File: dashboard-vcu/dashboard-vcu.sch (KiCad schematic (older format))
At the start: 23 parts, among them IC1 XL1509-5.0E1, J1 776163-1, U1 ATmega2560-16AU, Y1 Resonator

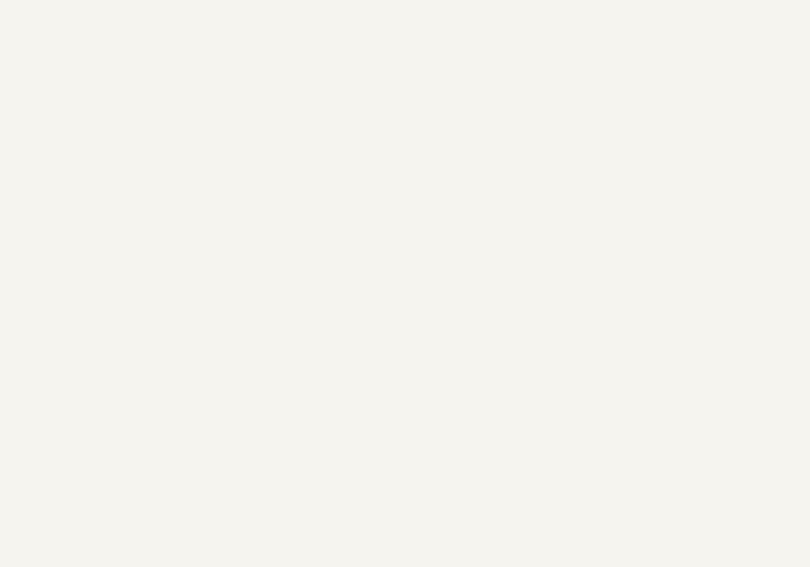
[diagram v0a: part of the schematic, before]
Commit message: dash tweaks
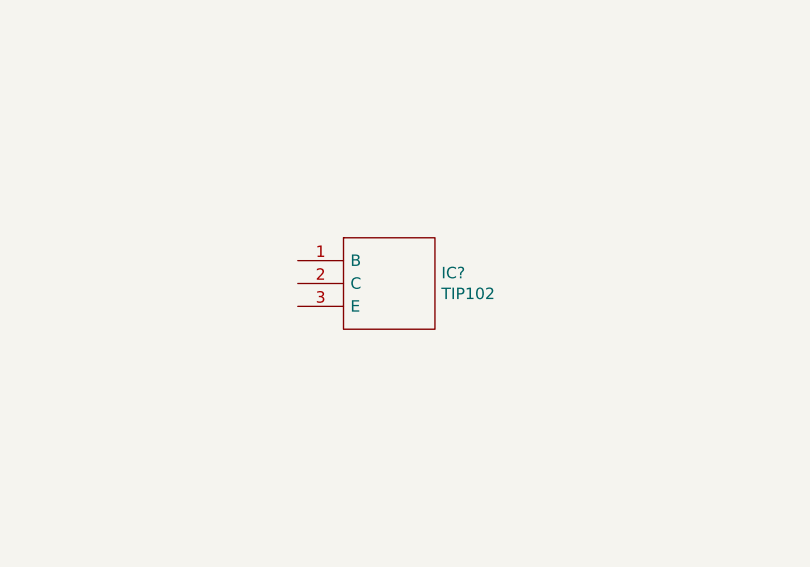
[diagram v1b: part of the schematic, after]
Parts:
- added IC?: TIP102, TO270P460X1020X2008-3P, symbol Transistor_BJT:TIP102
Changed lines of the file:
@@
 Text GLabel 1900 13600 0    50   Input ~ 0
 GND
+$Comp
+L Transistor_BJT:TIP102 IC?
+U 1 1 61BEAF3E
+P 11250 5750
+F 0 "IC?" H 11878 5696 50  0000 L CNN
+F 1 "TIP102" H 11878 5605 50  0000 L CNN
+F 2 "TO270P460X1020X2008-3P" H 11900 5850 50  0001 L CNN
+F 3 "http://www.st.com/web/en/resource/technical/document/datasheet/CD00001234.pdf" H 11900 5750 50  0001 L CNN
+F 4 "TIP102, Darlington Transistor, NPN 8 A 100 V HFE:200, 3-Pin, TO-220" H 11900 5650 50  0001 L CNN "Description"
+F 5 "4.6" H 11900 5550 50  0001 L CNN "Height"
+F 6 "STMicroelectronics" H 11900 5450 50  0001 L CNN "Manufacturer_Name"
+F 7 "TIP102" H 11900 5350 50  0001 L CNN "Manufacturer_Part_Number"
+F 8 "511-TIP102" H 11900 5250 50  0001 L CNN "Mouser Part Number"
+F 9 "https://www.mouser.co.uk/ProductDetail/STMicroelectronics/TIP102?qs=ljbEvF4DwONmWw0zLDYvVw%3D%3D" H 11900 5150 50  0001 L CNN "Mouser Price/Stock"
+F 10 "TIP102" H 11900 5050 50  0001 L CNN "Arrow Part Number"
+F 11 "https://www.arrow.com/en/products/tip102/stmicroelectronics?region=nac" H 11900 4950 50  0001 L CNN "Arrow Price/Stock"
+	1    11250 5750
+	1    0    0    -1
+$EndComp
 $EndSCHEMATC

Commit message: Tweaks
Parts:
- added IC3: TIP102, Package_TO_SOT_THT:TO270P460X1020X2008-3P, symbol Transistor_BJT:TIP102
- added J2: Conn_01x05_MountingPin, Connector_PinHeader_1.00mm:PinHeader_1x05_P1.00mm_Vertical, symbol Connector_Generic_MountingPin:Conn_01x05_MountingPin
- added R10, R11, R6, R7, R8, R9: 220, Resistor_SMD:R_0201_0603Metric, symbol Device:R_US
- added R4, R5: 2k2, Resistor_SMD:R_0201_0603Metric, symbol Device:R_US
- IC2: renamed from IC?; footprint TO270P460X1020X2008-3P -> Package_TO_SOT_THT:TO270P460X1020X2008-3P
- J1: footprint 7761631 -> Connector:7761631
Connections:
- net 12V: now also J1.1; no longer J1.29
- net 5V: now also J2.1 (Pin_1)
- net GND: now also IC2.3 (E), IC3.3 (E), J2.2 (Pin_2)
- net PWM2: now also R4.2
- net PWM3: now also R5.2
- net PWM4: now also R6.2
- net PWM5: now also R7.2
- net PWM6: now also R8.2
- net PWM7: now also R9.2
- net PWM8: now also R10.2
- net PWM9: now also R11.2
- net DTR: now reaches C1.2
- net DTR: now also J2.5 (Pin_5)
- net STATUS_A_R: now reaches J1.14
- net STATUS_A_R: now also R6.1
- net STATUS_A_G: now reaches J1.15
- net STATUS_A_G: now also R7.1
- net STATUS_A_B: now reaches J1.16
- net STATUS_A_B: now also R8.1
- net STATUS_B_R: now reaches J1.17
- net STATUS_B_R: now also R9.1
- net STATUS_B_G: now reaches J1.18
- net STATUS_B_G: now also R10.1
- net STATUS_B_B: now reaches J1.19
- net STATUS_B_B: now also R11.1
- net TEMP_GAUGE: now reaches J1.8
- net TEMP_GAUGE: now also IC3.2 (C)
- net FUEL_GAUGE: now reaches J1.9
- net FUEL_GAUGE: now also IC2.2 (C)
- net at IC2.1 (B): now also R4.1
- net PWM0 renamed RXD0
- net RXD0: now also J2.4 (Pin_4)
- net PWM1 renamed TXD0
- net TXD0: now also J2.3 (Pin_3)
- new net: IC3.1 (B), R5.1
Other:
- moved on the sheet: IC2

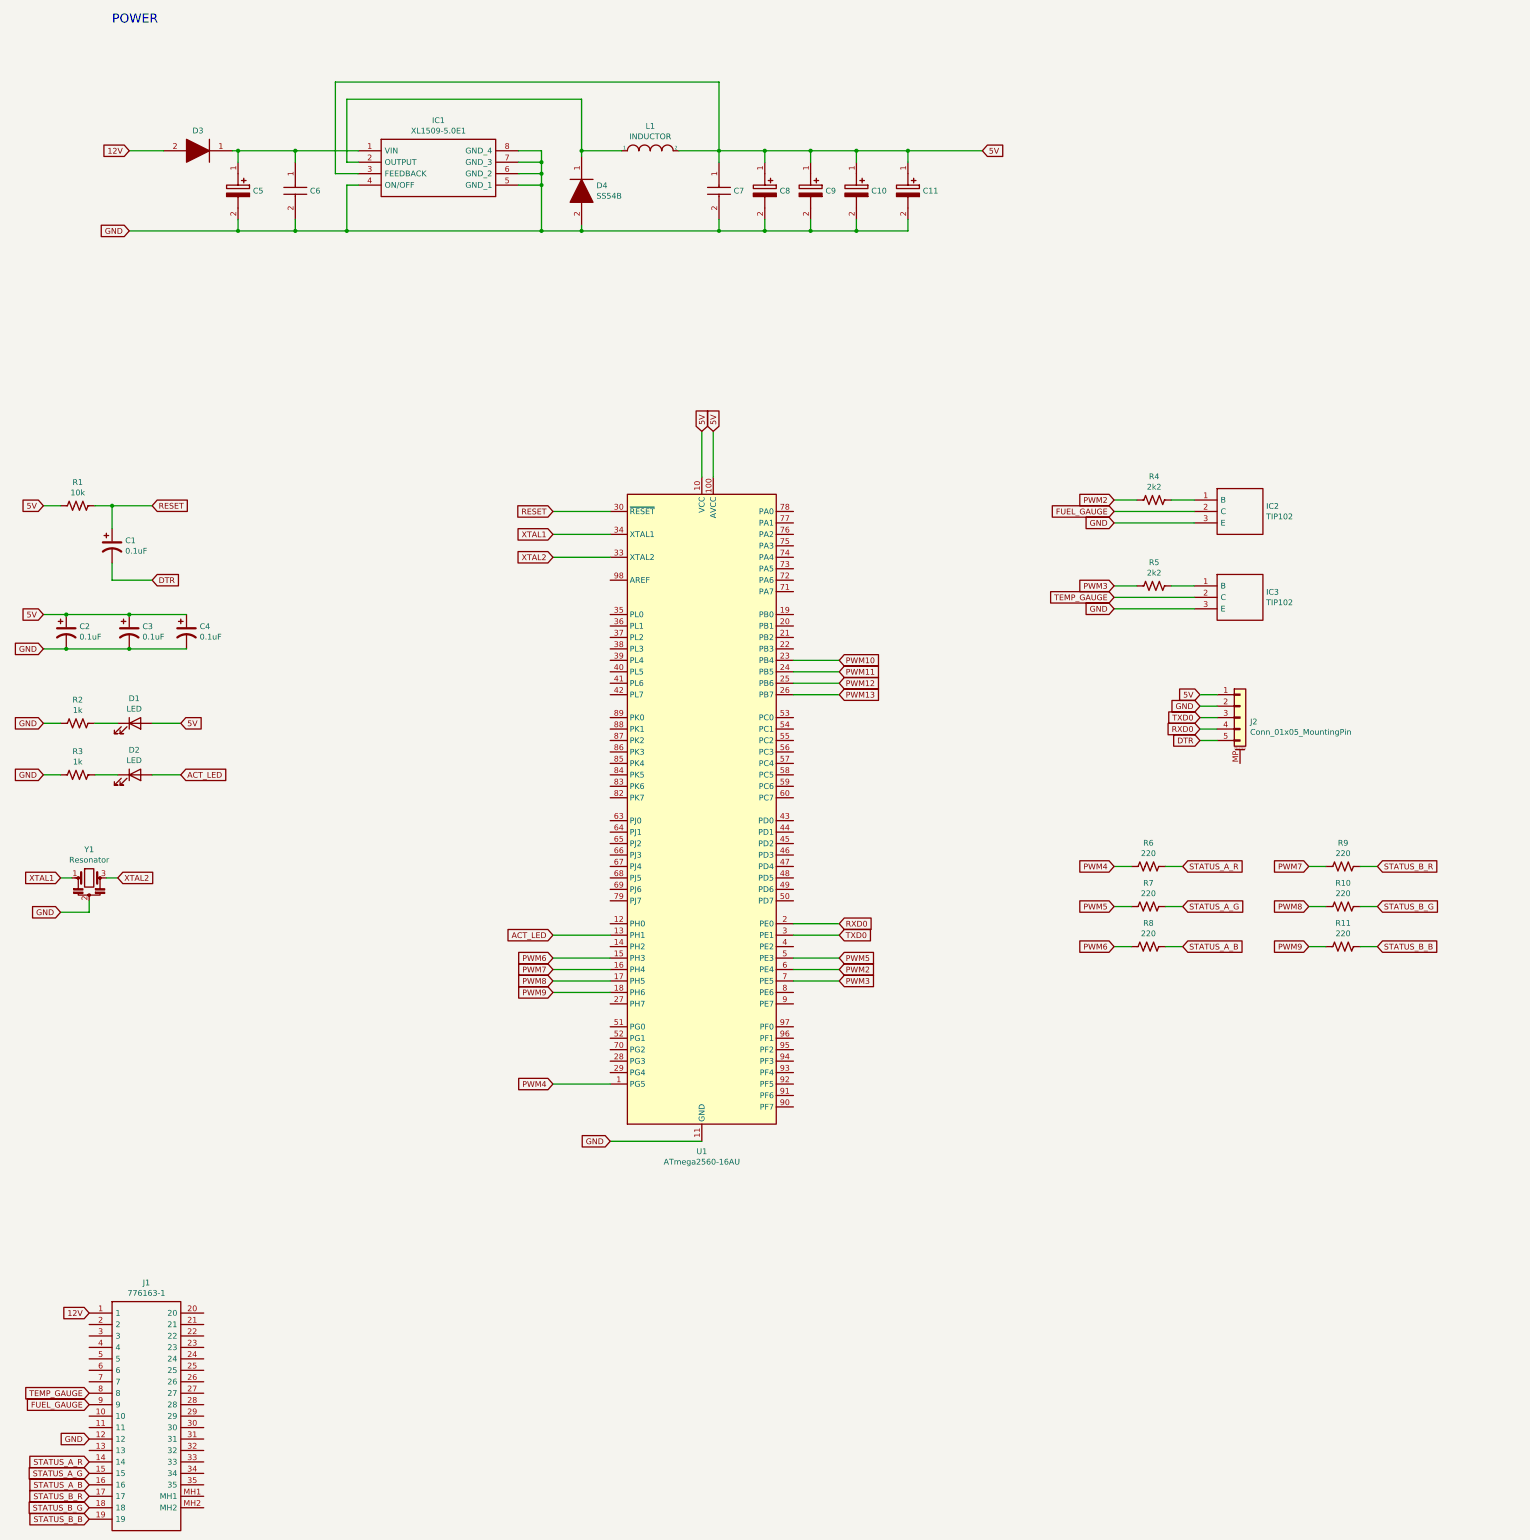
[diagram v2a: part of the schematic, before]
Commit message: Switch to using Pi Pico for dash vcu
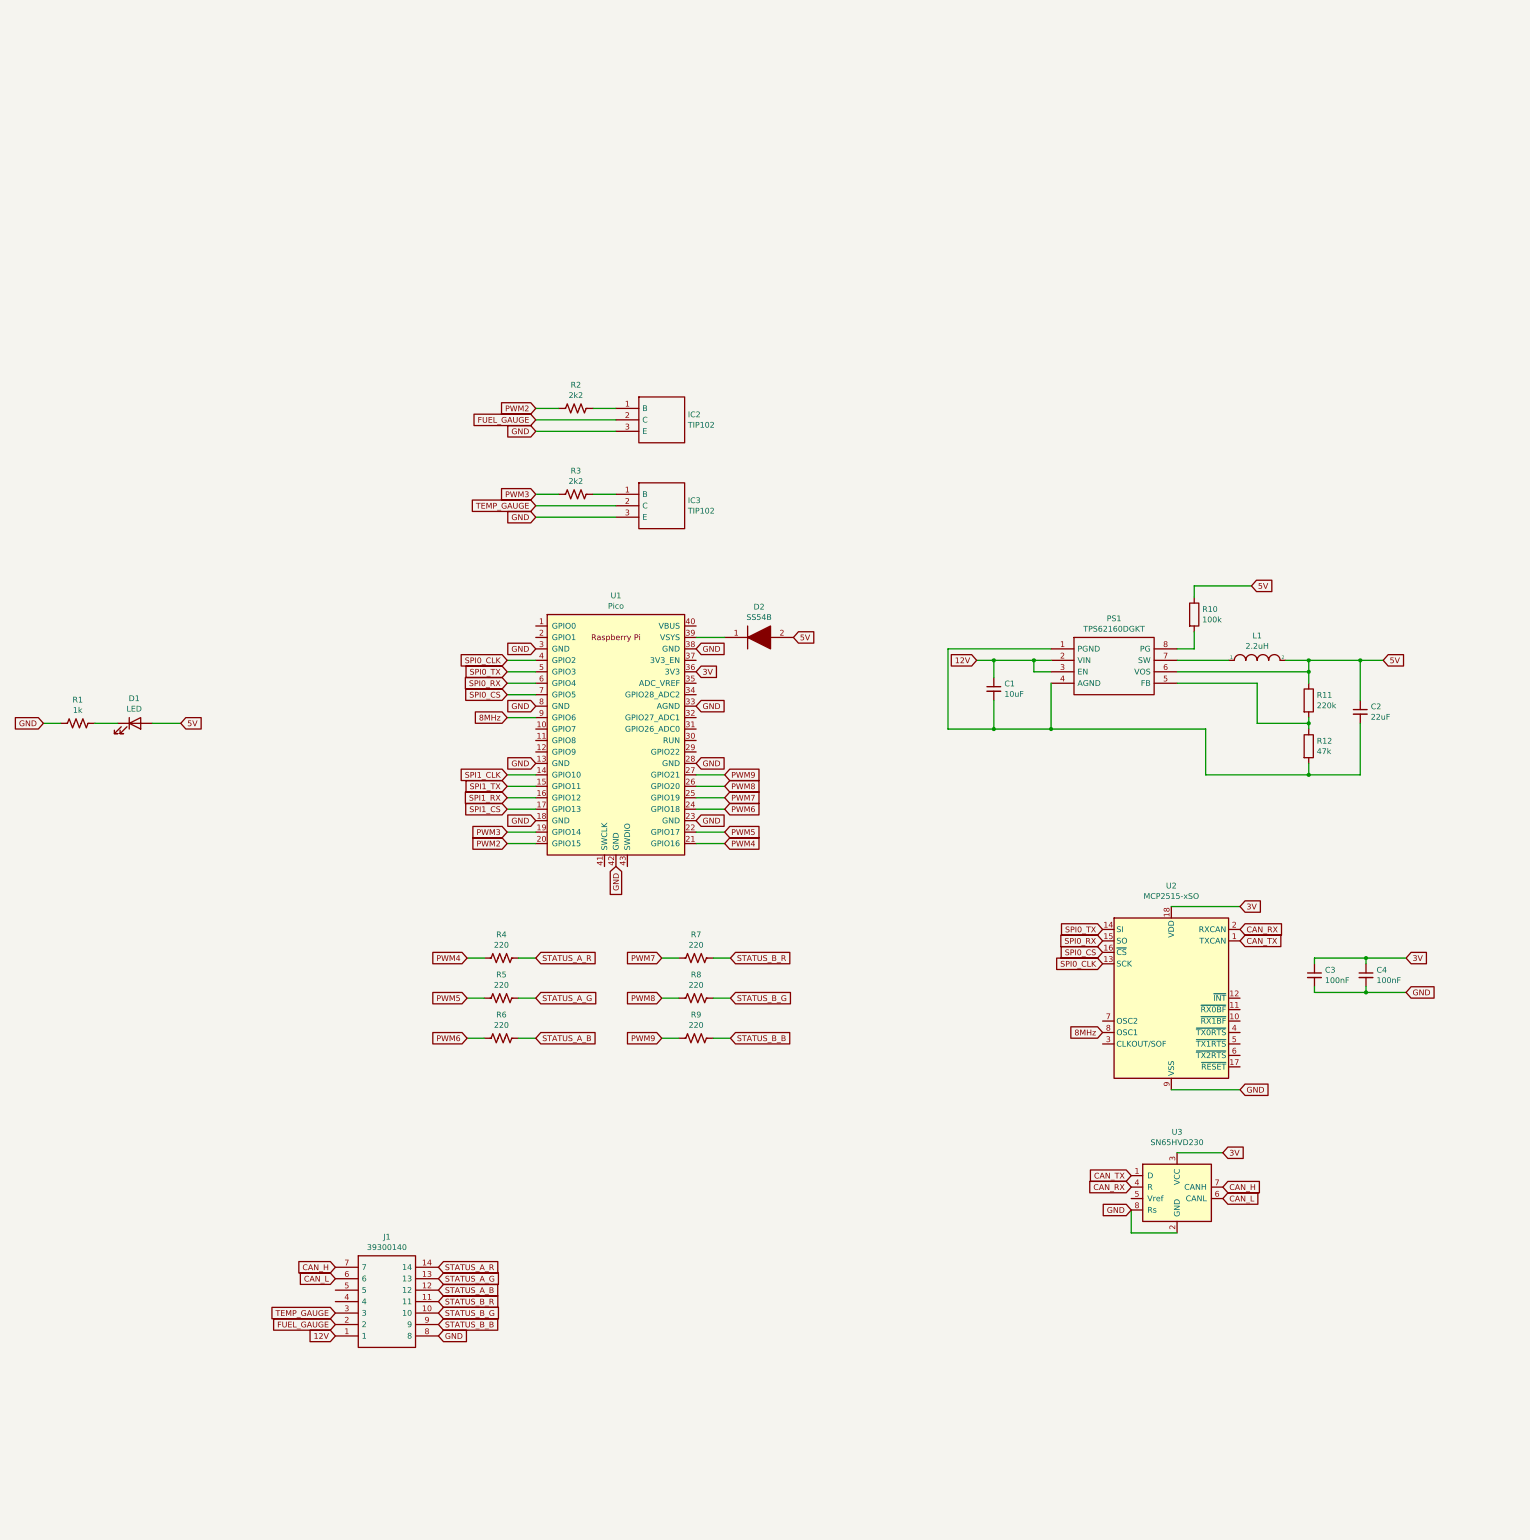
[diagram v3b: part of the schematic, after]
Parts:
- removed C1, C2, C3, C4: 0.1uF, Capacitor_SMD:RESC1005X55N, symbol Device:CP1
- removed C10, C11, C8, C9: TAJB107K006RNJV, Capacitor_SMD:CAPPM3528X210N, symbol Analog:TAJB107K006RNJV
- removed C5: VZH331M1ETT-0810, Capacitor_SMD:CAPAE830X1050N, symbol Analog:VZH331M1ETT-0810
- removed C6, C7: CL21B105KBFNNNE, Capacitor_SMD:CAPC2012X135N, symbol Analog:CL21B105KBFNNNE
- removed D2: LED, LED_SMD:LED_0603_1608Metric, symbol Device:LED
- removed D3, D4: SS54B, Diode_SMD:DIOM5336X244N, symbol Diode:SS54B
- removed IC1: XL1509-5.0E1, Package_SIP:SOIC127P600X175-8N, symbol power:XL1509-5.0E1
- removed J1: 776163-1, Connector:7761631, symbol Connector:776163-1
- removed J2: Conn_01x05_MountingPin, Connector_PinHeader_1.00mm:PinHeader_1x05_P1.00mm_Vertical, symbol Connector_Generic_MountingPin:Conn_01x05_MountingPin
- removed R1: 10k, Resistor_SMD:R_1206_3216Metric, symbol Device:R_US
- removed R3: 1k, Resistor_SMD:R_0201_0603Metric, symbol Device:R_US
- removed U1: ATmega2560-16AU, Package_QFP:TQFP-100_14x14mm_P0.5mm, symbol MCU_Microchip_ATmega:ATmega2560-16AU
- removed Y1: Resonator, RF:CSTNE16M0V530000R0, symbol Device:Resonator
- added C1: 10uF, Capacitor_SMD:C_0603_1608Metric, symbol Device:C_Small
- added C2: 22uF, Capacitor_SMD:C_0805_2012Metric, symbol Device:C_Small
- added C3, C4: 100nF, Capacitor_SMD:C_0603_1608Metric, symbol Device:C_Small
- added D2: SS54B, Diode_SMD:DIOM5336X244N, symbol Diode:SS54B
- added J1: 39300140, Connector:39300140, symbol Connector:39300140
- added PS1: TPS62160DGKT, Module:SOP65P490X110-8N, symbol MCU_Module:TPS62160DGKT
- added R10: 100k, Resistor_SMD:R_0201_0603Metric, symbol Device:R
- added R11: 220k, Resistor_SMD:R_0201_0603Metric, symbol Device:R
- added R12: 47k, Resistor_SMD:R_0201_0603Metric, symbol Device:R
- added U1: Pico, Module:RPi_Pico_SMD_TH, symbol MCU_Module:Pico
- added U2: MCP2515-xSO, Package_SO:SOIC-18W_7.5x11.6mm_P1.27mm, symbol Interface_CAN_LIN:MCP2515-xSO
- added U3: SN65HVD230, Package_SO:SOIC-8_3.9x4.9mm_P1.27mm, symbol Interface_CAN_LIN:SN65HVD230
- L1: value INDUCTOR -> 2.2uH; footprint (none) -> Inductor_SMD:NR6028T220M
- renumbered R2 to R1, R4 to R2, R5 to R3, R6 to R4, R7 to R5, R8 to R6, R9 to R7, R10 to R8, R11 to R9
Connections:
- net 12V: now also C1.1, J1.1, PS1.2 (VIN), PS1.3 (EN)
- net 5V: now also C2.1, D2.2, PS1.6 (VOS), R10.1, R11.1
- net FUEL_GAUGE: now also J1.2
- net GND: now also C3.2, C4.2, J1.8, U1.13 (GND), U1.18 (GND), U1.23 (GND), U1.28 (GND), U1.3 (GND), U1.33 (AGND), U1.38 (GND), U1.42 (GND), U1.8 (GND), U2.9 (VSS), U3.2 (GND), U3.8 (Rs)
- net PWM2: now also U1.20 (GPIO15)
- net PWM3: now also U1.19 (GPIO14)
- net PWM4: now also U1.21 (GPIO16)
- net PWM5: now also U1.22 (GPIO17)
- net PWM6: now also U1.24 (GPIO18)
- net PWM7: now also U1.25 (GPIO19)
- net PWM8: now also U1.26 (GPIO20)
- net PWM9: now also U1.27 (GPIO21)
- net STATUS_A_B: now also J1.12
- net STATUS_A_G: now also J1.13
- net STATUS_A_R: now also J1.14
- net STATUS_B_B: now also J1.9
- net STATUS_B_G: now also J1.10
- net STATUS_B_R: now also J1.11
- net TEMP_GAUGE: now also J1.3
- net at L1.1: now also PS1.7 (SW)
- new net: D2.1, U1.39 (VSYS)
- new net: C1.2, C2.2, PS1.1 (PGND), PS1.4 (AGND), R12.2
- new net: PS1.5 (FB), R11.2, R12.1
- new net: PS1.8 (PG), R10.2
- new net 3V: C3.1, C4.1, U1.36 (3V3), U2.18 (VDD), U3.3 (VCC)
- new net 8MHz: U1.9 (GPIO6), U2.8 (OSC1)
- new net CAN_H: J1.7, U3.7 (CANH)
- new net CAN_L: J1.6, U3.6 (CANL)
- new net CAN_RX: U2.2 (RXCAN), U3.4 (R)
- new net CAN_TX: U2.1 (TXCAN), U3.1 (D)
- new net SPI0_CLK: U1.4 (GPIO2), U2.13 (SCK)
- new net SPI0_CS: U1.7 (GPIO5), U2.16 (~CS)
- new net SPI0_RX: U1.6 (GPIO4), U2.15 (SO)
- new net SPI0_TX: U1.5 (GPIO3), U2.14 (SI)
- new net SPI1_CLK: U1.14 (GPIO10)
- new net SPI1_CS: U1.17 (GPIO13)
- new net SPI1_RX: U1.16 (GPIO12)
- new net SPI1_TX: U1.15 (GPIO11)
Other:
- note removed: "POWER"
- moved on the sheet: IC2, IC3, R2, R3, R4, R5, R6, R7, R8, R9
